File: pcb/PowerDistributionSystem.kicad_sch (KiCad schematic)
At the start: 42 parts, among them J1 JST-PH, J2 JST-PH, J3 JST-PH, J4 JST-PH, U1 TMC2209-LA-T, U2 D24V7F5, U3 D24V7F3

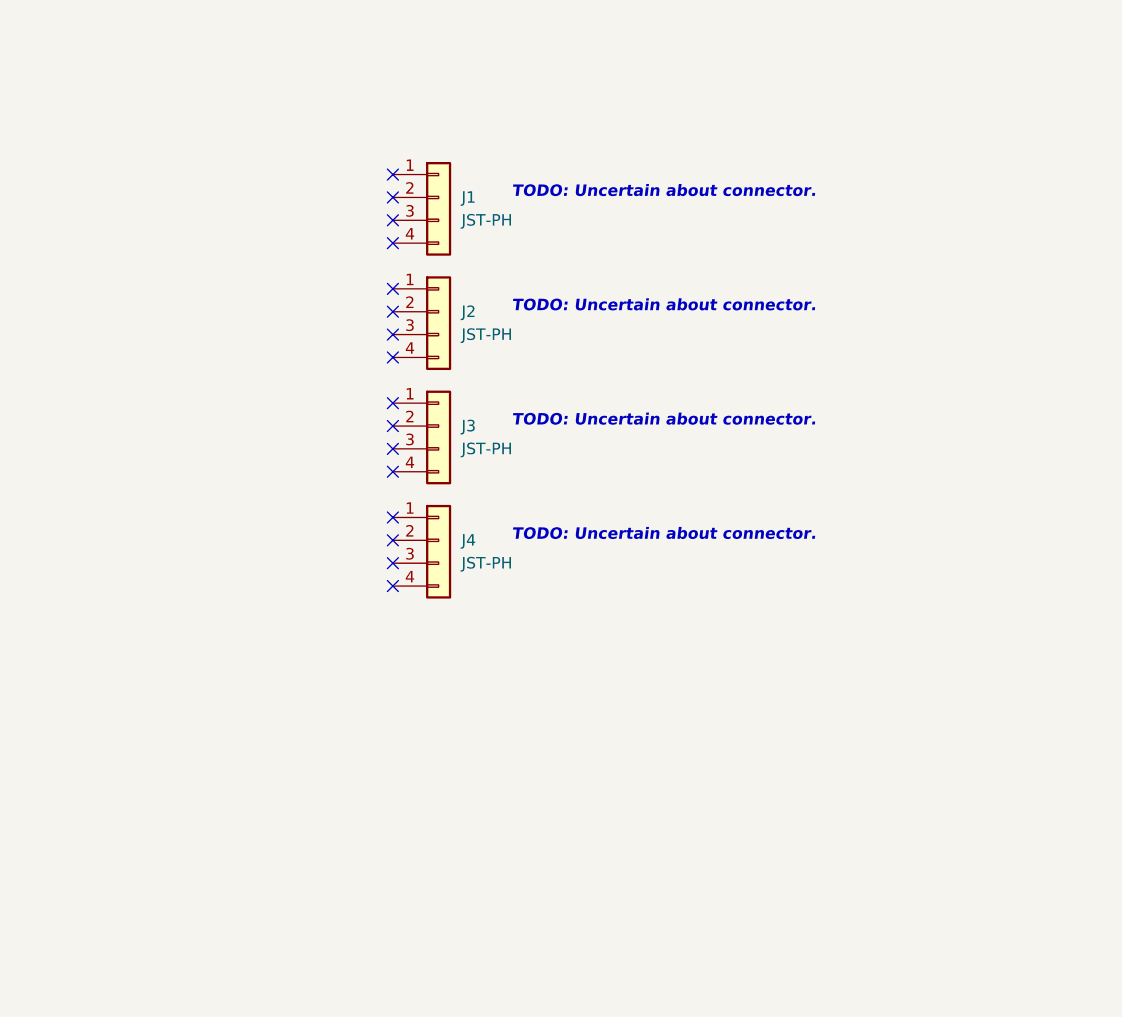
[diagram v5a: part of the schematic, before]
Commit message: Expanded upon the connectors.
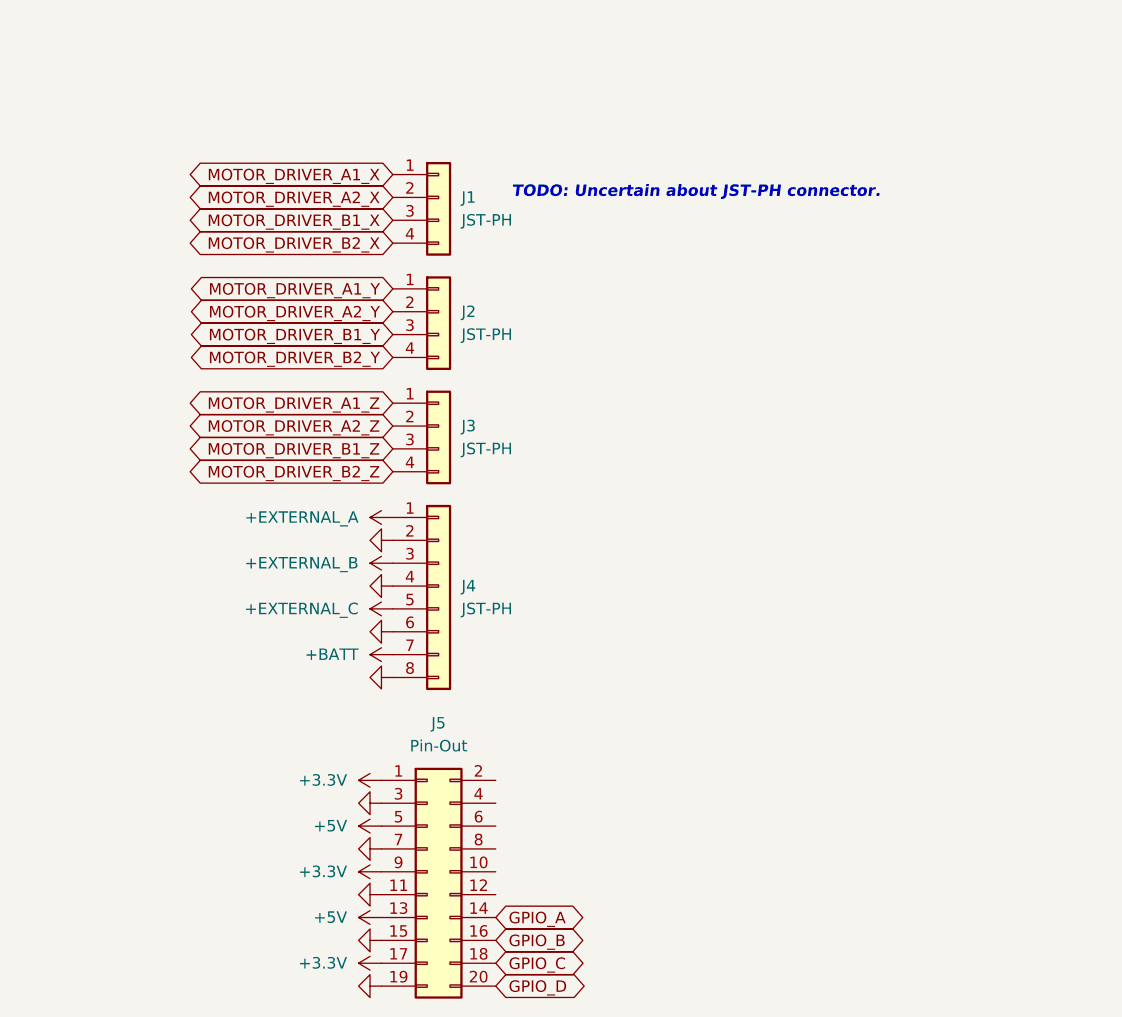
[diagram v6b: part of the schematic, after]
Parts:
- added J5: Pin-Out, Connector_IDC:IDC-Header_2x10_P2.54mm_Vertical, symbol Connector_Generic:Conn_02x10_Odd_Even
- J4: footprint Connector_JST:JST_PH_B4B-PH-K_1x04_P2.00mm_Vertical -> Connector_JST:JST_PH_B8B-PH-K_1x08_P2.00mm_Vertical; symbol Connector_Generic:Conn_01x04 -> Connector_Generic:Conn_01x08
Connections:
- net +3.3V: now also J5.1 (Pin_1), J5.17 (Pin_17), J5.9 (Pin_9)
- net +BATT: now also J4.7 (Pin_7)
- net GND: now also J4.2 (Pin_2), J4.4 (Pin_4), J4.6 (Pin_6), J4.8 (Pin_8), J5.11 (Pin_11), J5.15 (Pin_15), J5.19 (Pin_19), J5.3 (Pin_3), J5.7 (Pin_7)
- net MOTOR_DRIVER_A1_Y: now reaches J2.1 (Pin_1)
- net MOTOR_DRIVER_A2_Y: now reaches J2.2 (Pin_2)
- net MOTOR_DRIVER_B1_Y: now reaches J2.3 (Pin_3)
- net MOTOR_DRIVER_B2_Y: now reaches J2.4 (Pin_4)
- net +EXTERNAL_A: now reaches J4.1 (Pin_1)
- net +EXTERNAL_B: now reaches J4.3 (Pin_3)
- net MOTOR_DRIVER_A1_Z: now reaches J3.1 (Pin_1)
- net MOTOR_DRIVER_A2_Z: now reaches J3.2 (Pin_2)
- net MOTOR_DRIVER_B1_Z: now reaches J3.3 (Pin_3)
- net MOTOR_DRIVER_B2_Z: now reaches J3.4 (Pin_4)
- net MOTOR_DRIVER_A1_X: now reaches J1.1 (Pin_1)
- net MOTOR_DRIVER_A2_X: now reaches J1.2 (Pin_2)
- net MOTOR_DRIVER_B1_X: now reaches J1.3 (Pin_3)
- net MOTOR_DRIVER_B2_X: now reaches J1.4 (Pin_4)
- new net +5V: J5.13 (Pin_13), J5.5 (Pin_5)
- new net +EXTERNAL_C: J4.5 (Pin_5)
- new net GPIO_A: J5.14 (Pin_14)
- new net GPIO_B: J5.16 (Pin_16)
- new net GPIO_C: J5.18 (Pin_18)
- new net GPIO_D: J5.20 (Pin_20)
- no-connect marks 37 -> 21
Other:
- note added: "TODO: Uncertain about JST-PH connector."
- note removed: "TODO: Uncertain about connector."

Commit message: Made hierarchal sheets for stepper motor drivers.
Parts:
- removed C1, C2, C4, C8: 100n, Capacitor_SMD:C_1206_3216Metric_Pad1.33x1.80mm_HandSolder, symbol Device:C_Small
- removed C3: 25TGV100M8X10.5, Capacitor_SMD:CP_Elec_8x10.5, symbol Device:C_Polarized
- removed C5: 2u2, Capacitor_SMD:C_1206_3216Metric_Pad1.33x1.80mm_HandSolder, symbol Device:C_Small
- removed C6: 22n, Capacitor_SMD:C_1206_3216Metric_Pad1.33x1.80mm_HandSolder, symbol Device:C_Small
- removed D1: YELLOW, LED_SMD:LED_1206_3216Metric_Pad1.42x1.75mm_HandSolder, symbol Device:LED
- removed R1, R2: RL1206FR-070R05L, Resistor_SMD:R_1206_3216Metric_Pad1.30x1.75mm_HandSolder, symbol Device:R
- removed R3: 2k, Resistor_SMD:R_1206_3216Metric_Pad1.30x1.75mm_HandSolder, symbol Device:R
- removed R4: 1k, Resistor_SMD:R_1206_3216Metric_Pad1.30x1.75mm_HandSolder, symbol Device:R
- removed R5: 20k, Resistor_SMD:R_1206_3216Metric_Pad1.30x1.75mm_HandSolder, symbol Device:R
- removed R6: 33k, Resistor_SMD:R_1206_3216Metric_Pad1.30x1.75mm_HandSolder, symbol Device:R
- removed RV1: 10k, pcb:TRIM_35WR10KLFTR, symbol Device:R_Potentiometer
- removed TP1, TP2, TP3: TestPoint, TestPoint:TestPoint_Pad_1.0x1.0mm, symbol Connector:TestPoint
- removed U1: TMC2209-LA-T, Package_DFN_QFN:VQFN-28-1EP_5x5mm_P0.5mm_EP3.7x3.7mm_ThermalVias, symbol Driver_Motor:TMC2209-LA
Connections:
- no-connect marks 21 -> 53
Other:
- added sheet Stepper Motor Driver - X (Stepper_Motor_Driver_TMC2209.kicad_sch)
- added sheet Stepper Motor Driver - Y (Stepper_Motor_Driver_TMC2209.kicad_sch)
- added sheet Stepper Motor Driver - Z (Stepper_Motor_Driver_TMC2209.kicad_sch)
- note removed: ""Attach 2.2μF to 4.7μF ceramic capacitor to GND near to pin for best performance." Note that Adafruit deviates and uses 10uF. @/pg 4/fig 1.1/`TMC2209`. @/pg 9/tbl 2.2/`TMC2209`."
- note removed: ""Tie to CPO using 22nF 50V capacitor." @/pg 4/fig 1.1/`TMC2209`. @/pg 9/tbl 2.2/`TMC2209`."
- note removed: ""Tie to GND using short wire for internal clock..." This is what the Adafruit breakout board also does. @/pg 8/sec 1.9/`TMC2209`. @/pg 9/tbl 2.2/`TMC2209`."
- note removed: ""Tie to VS using 100nF capacitor." Note that Adafruit deviates from this by using 220nF for their breakout board instead. Not sure why. @/pg 4/fig 1.1/`TMC2209`. @/pg 9/tbl 2.2/`TMC2209`."
- note removed: "@/pg 4/fig 1.1/`TMC2209`."
- note removed: "Can be left unused according to Adafruit's design."
- note removed: "Reference design: @/url:`github.com/adafruit/Adafruit-TMC2209-Breakout-PCB`."
- note removed: "TODO: No 22nF in book."
- note removed: "TODO: Not sure how important VREF is."
- note removed: "TODO: Not sure what these guys do."
- note removed: "TODO: Simplex UART? @/pg 82/fig 21.4/`TMC2209`."
- note removed: "TODO: Tests should be done on what happens if the stepper motors are turned."
